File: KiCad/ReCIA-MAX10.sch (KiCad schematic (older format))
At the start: 15 parts, among them J1 Conn_02x03_Odd_Even, U1 AMS1117-3.3, U2 SN74CBT16210, U3 SN74CBT16210, U4 10M02SCU169, U5 8520_DIP_SOCKET

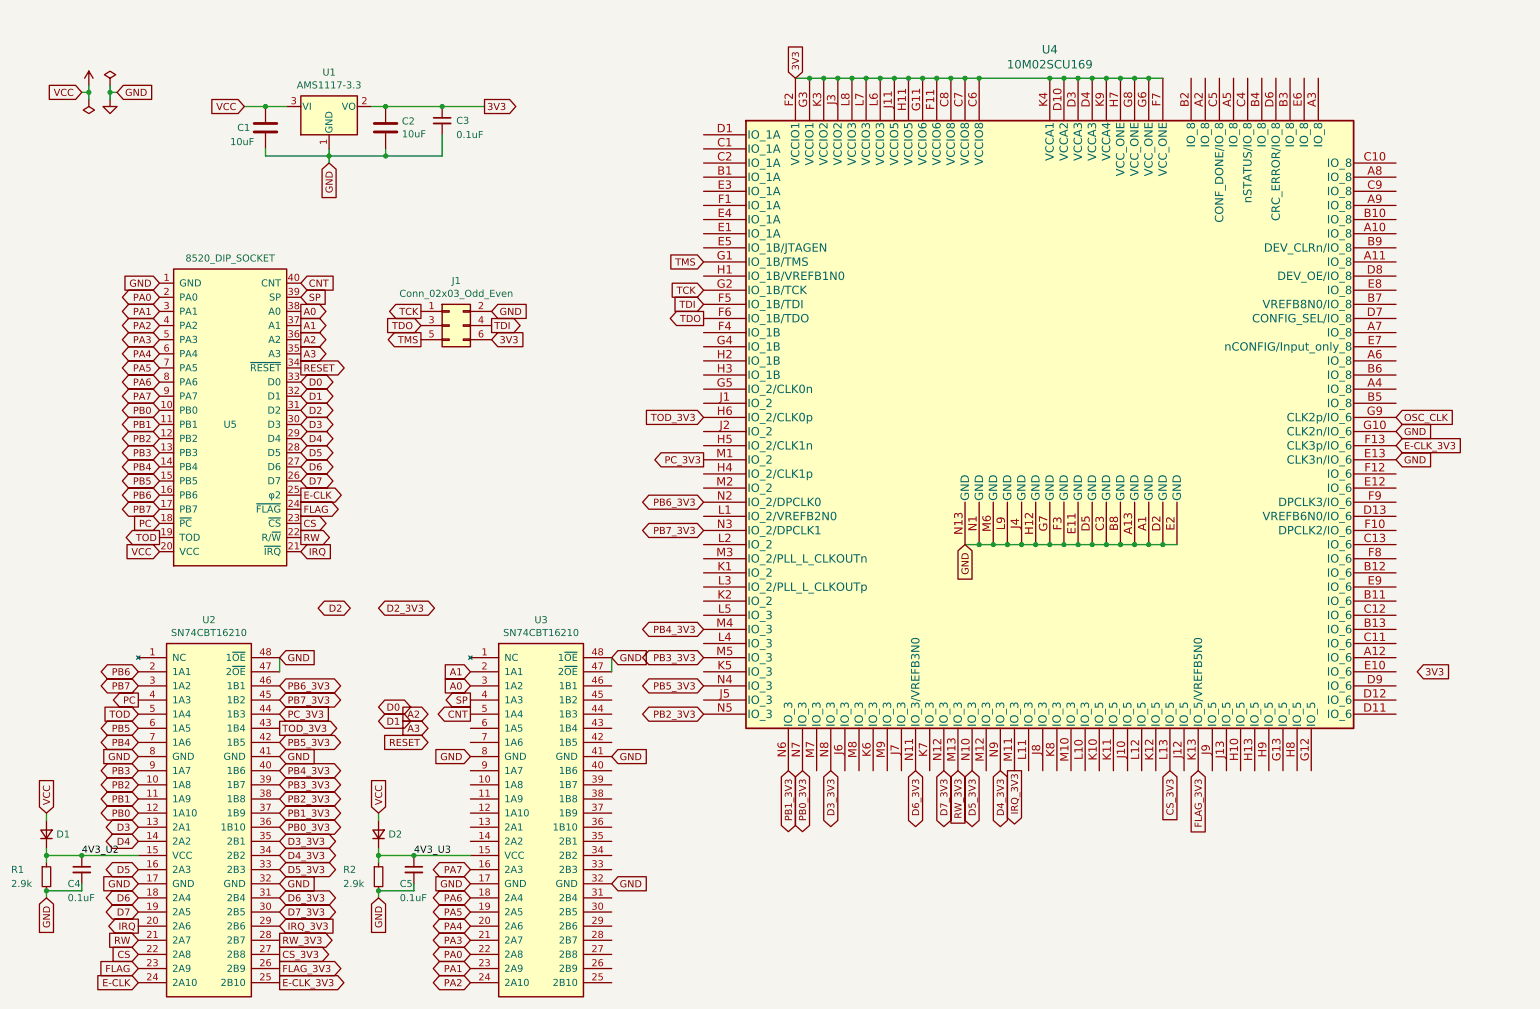
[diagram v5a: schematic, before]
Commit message: add XTAL to design
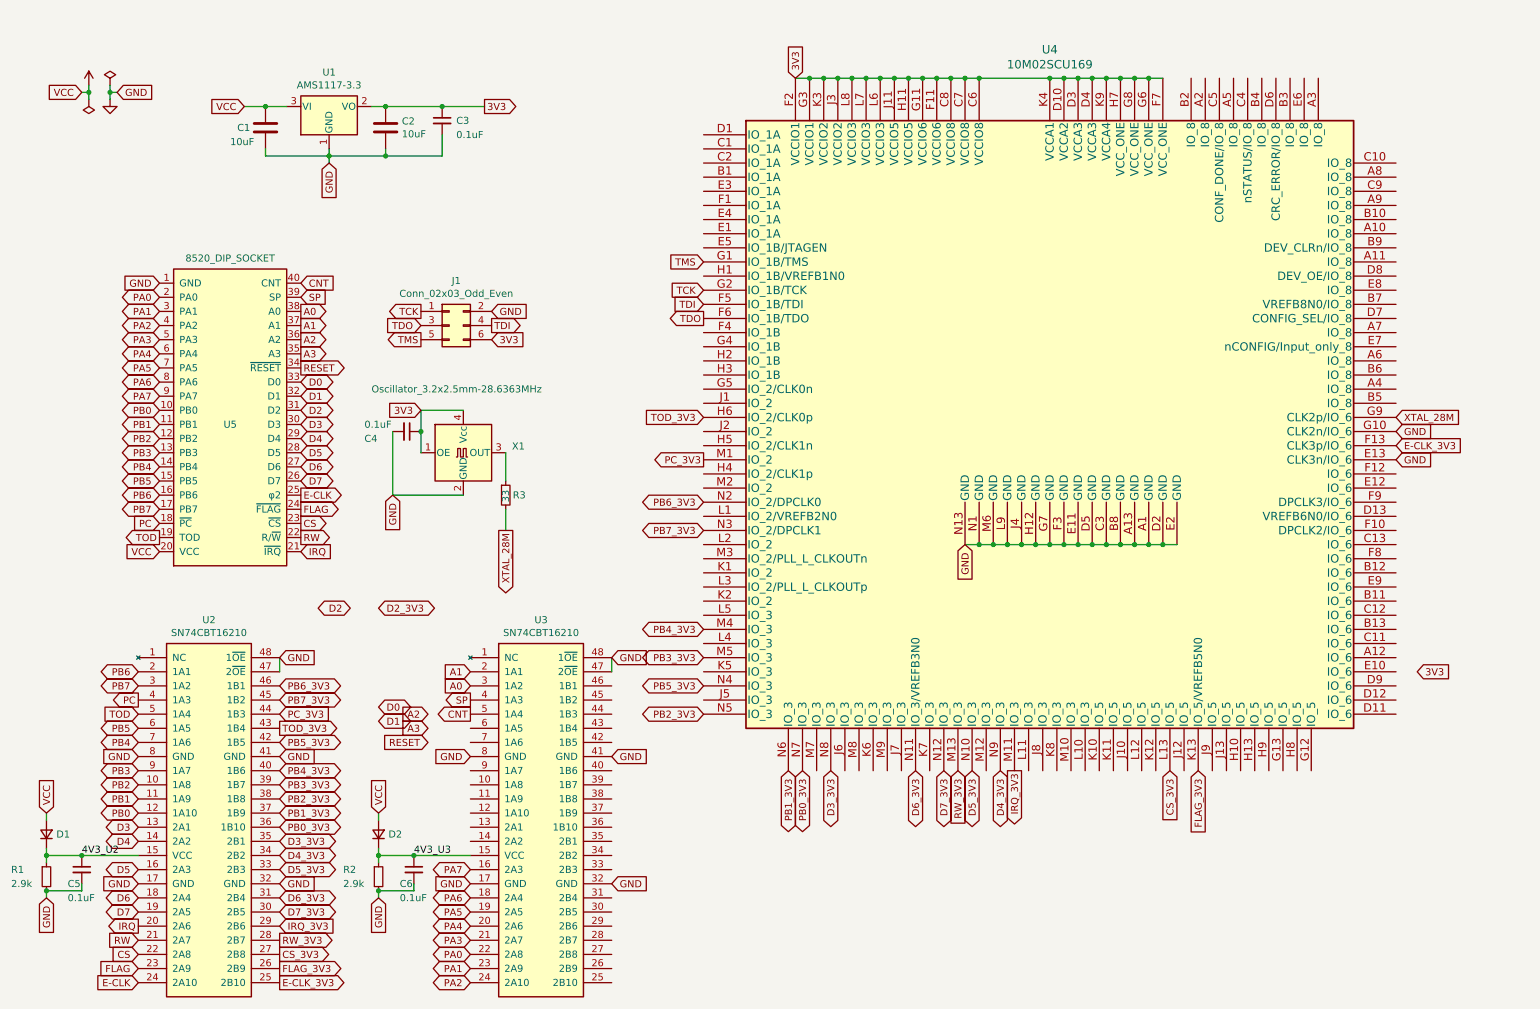
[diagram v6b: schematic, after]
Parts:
- added C4: 0.1uF, Capacitor_SMD:C_0805_2012Metric, symbol Device:C_Small
- added R3: 33, Resistor_SMD:R_0603_1608Metric_Pad0.98x0.95mm_HandSolder, symbol Device:R_Small
- added X1: Oscillator_3.2x2.5mm-28.6363MHz, Oscillator:Oscillator_SMD_SeikoEpson_SG8002CE-4Pin_3.2x2.5mm, symbol Oscillator:SG-8002CE
- R1, R2: footprint Capacitor_SMD:C_0603_1608Metric_Pad1.08x0.95mm_HandSolder -> Resistor_SMD:R_0603_1608Metric_Pad0.98x0.95mm_HandSolder
- renumbered C4 to C5, C5 to C6
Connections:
- net 3V3: now also C4.1, X1.1 (OE), X1.4 (Vcc)
- net GND: now also C4.2, X1.2 (GND)
- net OSC_CLK renamed XTAL_28M
- net XTAL_28M: now also R3.2
- new net: R3.1, X1.3 (OUT)
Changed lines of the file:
@@
 F 0 "R1" H 500 6750 50  0000 L CNN
 F 1 "2.9k" H 500 6650 50  0000 L CNN
-F 2 "Capacitor_SMD:C_0603_1608Metric_Pad1.08x0.95mm_HandSolder" H 750 6700 50  0001 C CNN
+F 2 "Resistor_SMD:R_0603_1608Metric_Pad0.98x0.95mm_HandSolder" H 750 6700 50  0001 C CNN
 F 3 "~" H 750 6700 50  0001 C CNN
 	1    750  6700
@@
 	750  6550 750  6600
 $Comp
-L Device:C_Small C4
+L Device:C_Small C5
 U 1 1 66D9BFBA
 P 1000 6650
-F 0 "C4" H 900 6550 50  0000 L CNN
+F 0 "C5" H 900 6550 50  0000 L CNN
 F 1 "0.1uF" H 900 6450 50  0000 L CNN
 F 2 "Capacitor_SMD:C_0603_1608Metric_Pad1.08x0.95mm_HandSolder" H 1000 6650 50  0001 C CNN
@@
 F 0 "R2" H 2850 6750 50  0000 L CNN
 F 1 "2.9k" H 2850 6650 50  0000 L CNN
-F 2 "Capacitor_SMD:C_0603_1608Metric_Pad1.08x0.95mm_HandSolder" H 3100 6700 50  0001 C CNN
+F 2 "Resistor_SMD:R_0603_1608Metric_Pad0.98x0.95mm_HandSolder" H 3100 6700 50  0001 C CNN
 F 3 "~" H 3100 6700 50  0001 C CNN
 	1    3100 6700
@@
 	3100 6550 3100 6600
 $Comp
-L Device:C_Small C5
+L Device:C_Small C6
 U 1 1 66E2D70C
 P 3350 6650
-F 0 "C5" H 3250 6550 50  0000 L CNN
+F 0 "C6" H 3250 6550 50  0000 L CNN
 F 1 "0.1uF" H 3250 6450 50  0000 L CNN
 F 2 "Capacitor_SMD:C_0603_1608Metric_Pad1.08x0.95mm_HandSolder" H 3350 6650 50  0001 C CNN
@@
 Text GLabel 5400 3450 0    50   Input ~ 0
 TOD_3V3
+Text GLabel 10300 3550 2    50   Input ~ 0
+GND
+$Comp
+L Oscillator:SG-8002CE X1
+U 1 1 66F84126
+P 3700 3700
+F 0 "X1" H 4044 3746 50  0000 L CNN
+F 1 "Oscillator_3.2x2.5mm-28.6363MHz" H 3050 4150 50  0000 L CNN
+F 2 "Oscillator:Oscillator_SMD_SeikoEpson_SG8002CE-4Pin_3.2x2.5mm" H 4400 3350 50  0001 C CNN
+F 3 "https://support.epson.biz/td/api/doc_check.php?mode=dl&lang=en&Parts=SG-8002DC" H 3600 3700 50  0001 C CNN
+	1    3700 3700
+	1    0    0    -1
+$EndComp
+Text GLabel 3400 3400 0    50   Input ~ 0
+3V3
+Wire Wire Line
+	3700 3400 3400 3400
+Wire Wire Line
+	3400 3400 3400 3550
+$Comp
+L Device:C_Small C4
+U 1 1 66FA138D
+P 3300 3550
+F 0 "C4" V 3350 3250 50  0000 L CNN
+F 1 "0.1uF" V 3250 3250 50  0000 L CNN
+F 2 "Capacitor_SMD:C_0805_2012Metric" H 3300 3550 50  0001 C CNN
+F 3 "~" H 3300 3550 50  0001 C CNN
+	1    3300 3550
+	0    1    1    0
+$EndComp
+Connection ~ 3400 3550
+Wire Wire Line
+	3400 3550 3400 3700
+Wire Wire Line
+	3200 3550 3200 4000
+Wire Wire Line
+	3200 4000 3700 4000
+Text GLabel 3200 4000 3    50   Input ~ 0
+GND
+Text GLabel 4000 4250 3    50   Output ~ 0
+XTAL_28M
+Wire Wire Line
+	4000 3700 4000 3900
+$Comp
+L Device:R_Small R3
+U 1 1 66FDE051
+P 4000 4000
+F 0 "R3" H 4050 4000 50  0000 L CNN
+F 1 "33" V 4000 3950 50  0000 L CNN
+F 2 "Resistor_SMD:R_0603_1608Metric_Pad0.98x0.95mm_HandSolder" H 4000 4000 50  0001 C CNN
+F 3 "~" H 4000 4000 50  0001 C CNN
+	1    4000 4000
+	1    0    0    -1
+$EndComp
+Wire Wire Line
+	4000 4100 4000 4250
 Text GLabel 10300 3450 2    50   Input ~ 0
-OSC_CLK
-Text GLabel 10300 3550 2    50   Input ~ 0
-GND
+XTAL_28M
 $EndSCHEMATC

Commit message: more routing, pin assignments and silkscreen fixes
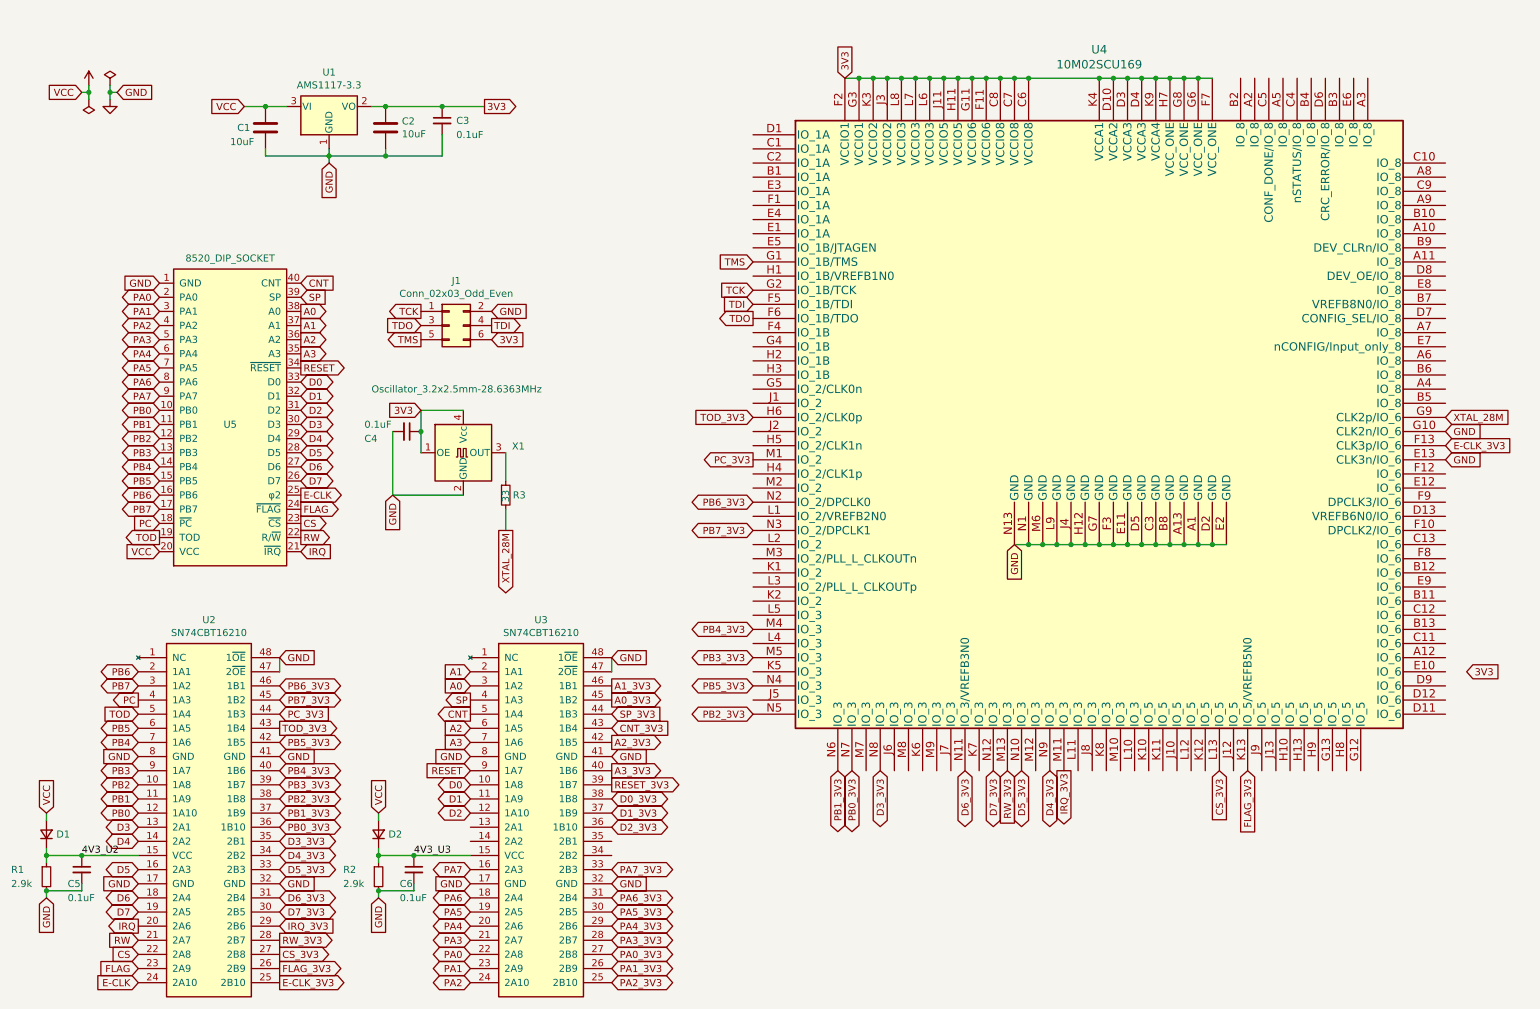
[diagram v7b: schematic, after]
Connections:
- net A2: now also U3.6 (1A5)
- net A3: now also U3.7 (1A6)
- net D0: now also U3.10 (1A8)
- net D1: now also U3.11 (1A9)
- net D2: now also U3.12 (1A10)
- net D2_3V3: now also U3.36 (1B10)
- net RESET: now also U3.9 (1A7)
- net PA2_3V3: now reaches U3.25 (2B10)
- net PA1_3V3: now reaches U3.26 (2B9)
- net PA0_3V3: now reaches U3.27 (2B8)
- net PA3_3V3: now reaches U3.28 (2B7)
- net PA4_3V3: now reaches U3.29 (2B6)
- net PA5_3V3: now reaches U3.30 (2B5)
- net PA6_3V3: now reaches U3.31 (2B4)
- net PA7_3V3: now reaches U3.33 (2B3)
- net D1_3V3: now reaches U3.37 (1B9)
- net D0_3V3: now reaches U3.38 (1B8)
- net RESET_3V3: now reaches U3.39 (1B7)
- net A3_3V3: now reaches U3.40 (1B6)
- net A2_3V3: now reaches U3.42 (1B5)
- net CNT_3V3: now reaches U3.43 (1B4)
- net SP_3V3: now reaches U3.44 (1B3)
- net A0_3V3: now reaches U3.45 (1B2)
- net A1_3V3: now reaches U3.46 (1B1)
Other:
- moved on the sheet: U4

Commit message: more pin assignments and routing
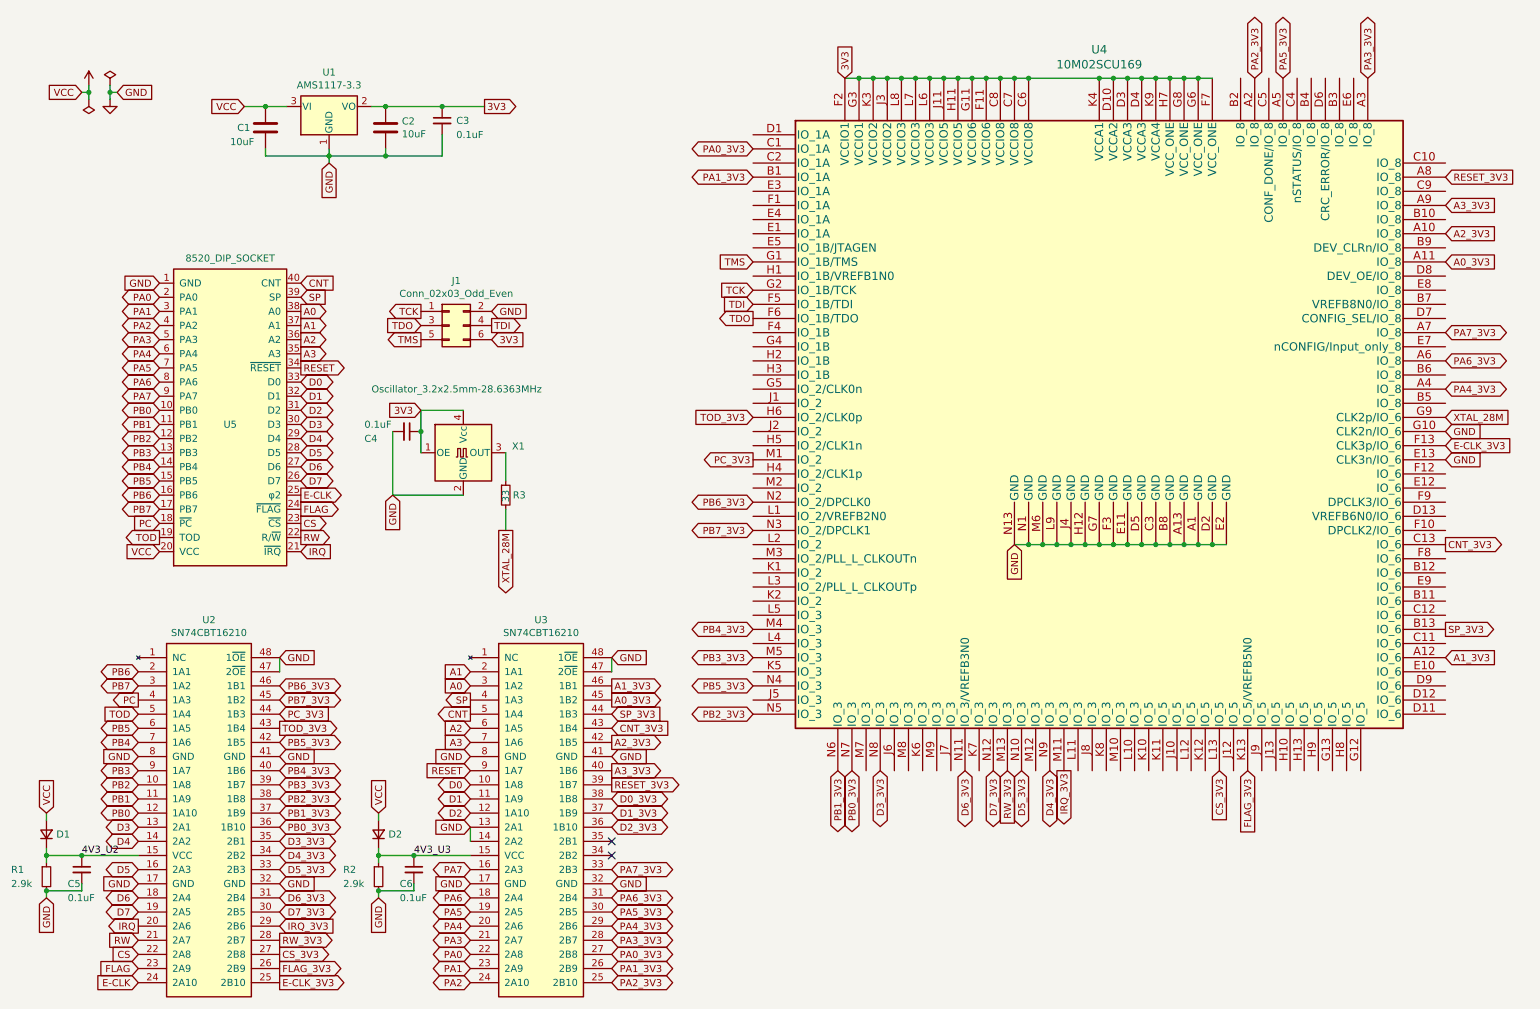
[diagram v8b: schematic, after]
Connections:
- net A0_3V3: now also U4.A11 (IO_8)
- net A1_3V3: now also U4.A12 (IO_6)
- net A2_3V3: now also U4.A10 (IO_8)
- net A3_3V3: now also U4.A9 (IO_8)
- net CNT_3V3: now also U4.C13 (IO_6)
- net GND: now also U3.13 (2A1), U3.14 (2A2)
- net PA0_3V3: now also U4.C1 (IO_1A)
- net PA1_3V3: now also U4.B1 (IO_1A)
- net PA2_3V3: now also U4.A2 (IO_8)
- net PA3_3V3: now also U4.A3 (IO_8)
- net PA4_3V3: now also U4.A4 (IO_8)
- net PA5_3V3: now also U4.A5 (IO_8)
- net PA6_3V3: now also U4.A6 (IO_8)
- net PA7_3V3: now also U4.A7 (IO_8)
- net RESET_3V3: now also U4.A8 (IO_8)
- net SP_3V3: now also U4.B13 (IO_6)
- no-connect marks 0 -> 2
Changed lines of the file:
@@
 Wire Wire Line
 	8900 1050 9000 1050
-Text GLabel 10800 5250 2    50   Input ~ 0
-3V3
 $Comp
 L ReCIA:SN74CBT16210 U2
@@
 Text GLabel 4750 7450 2    50   BiDi ~ 0
 PA2_3V3
+Text GLabel 3750 6350 0    50   Input ~ 0
+GND
+Wire Wire Line
+	3750 6350 3750 6450
+NoConn ~ 4750 6450
+NoConn ~ 4750 6550
+Text GLabel 10650 5150 2    50   Input ~ 0
+A1_3V3
+Text GLabel 10650 2350 2    50   Input ~ 0
+A0_3V3
+Text GLabel 10650 2150 2    50   Input ~ 0
+A2_3V3
+Text GLabel 10650 1950 2    50   Input ~ 0
+A3_3V3
+Text GLabel 10650 1750 2    50   Input ~ 0
+RESET_3V3
+Text GLabel 10650 4350 2    50   Output ~ 0
+CNT_3V3
+Text GLabel 10650 4950 2    50   Output ~ 0
+SP_3V3
+Text GLabel 10650 2850 2    50   BiDi ~ 0
+PA7_3V3
+Text GLabel 10650 3050 2    50   BiDi ~ 0
+PA6_3V3
+Text GLabel 9500 1050 1    50   BiDi ~ 0
+PA5_3V3
+Text GLabel 10650 3250 2    50   BiDi ~ 0
+PA4_3V3
+Text GLabel 10100 1050 1    50   BiDi ~ 0
+PA3_3V3
+Text GLabel 5750 1550 0    50   BiDi ~ 0
+PA0_3V3
+Text GLabel 5750 1750 0    50   BiDi ~ 0
+PA1_3V3
+Text GLabel 9300 1050 1    50   BiDi ~ 0
+PA2_3V3
 $EndSCHEMATC
